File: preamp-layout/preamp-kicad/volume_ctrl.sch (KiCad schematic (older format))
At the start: 82 parts, among them J38 Conn_01x03_Male, J50 Conn_01x03_Male, J51 Conn_01x02_Male, J52 Conn_01x03_Male, J54 Conn_01x03_Male, J55 Conn_01x02_Male, J56 Conn_01x03_Male, J57 Conn_01x02_Male, U11 DAC5574, U12 TL074CDR, U13 NJM2068M, U14 THAT2181, U15 THAT2181, U16 NJM2068M, U17 THAT2181, U18 THAT2181

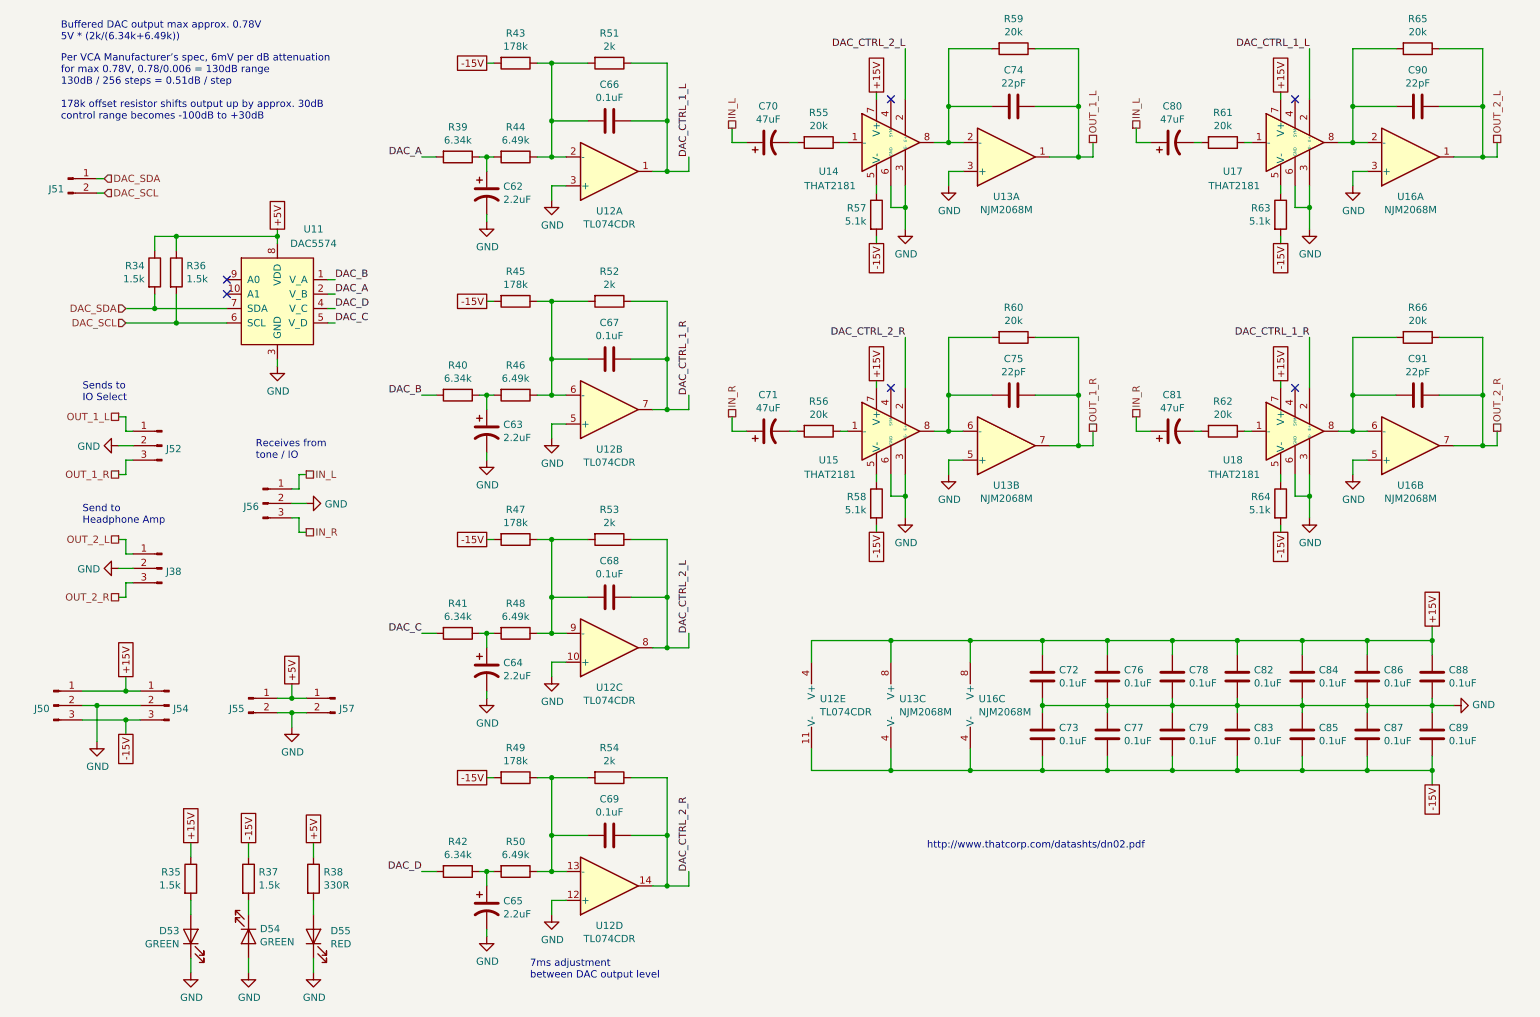
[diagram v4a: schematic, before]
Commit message: Balanced in/out update
Created THAT1646, THAT1280 schematic symbols an implemented in the balanced IO daughter card. Various layout updates as well, this is WIP.
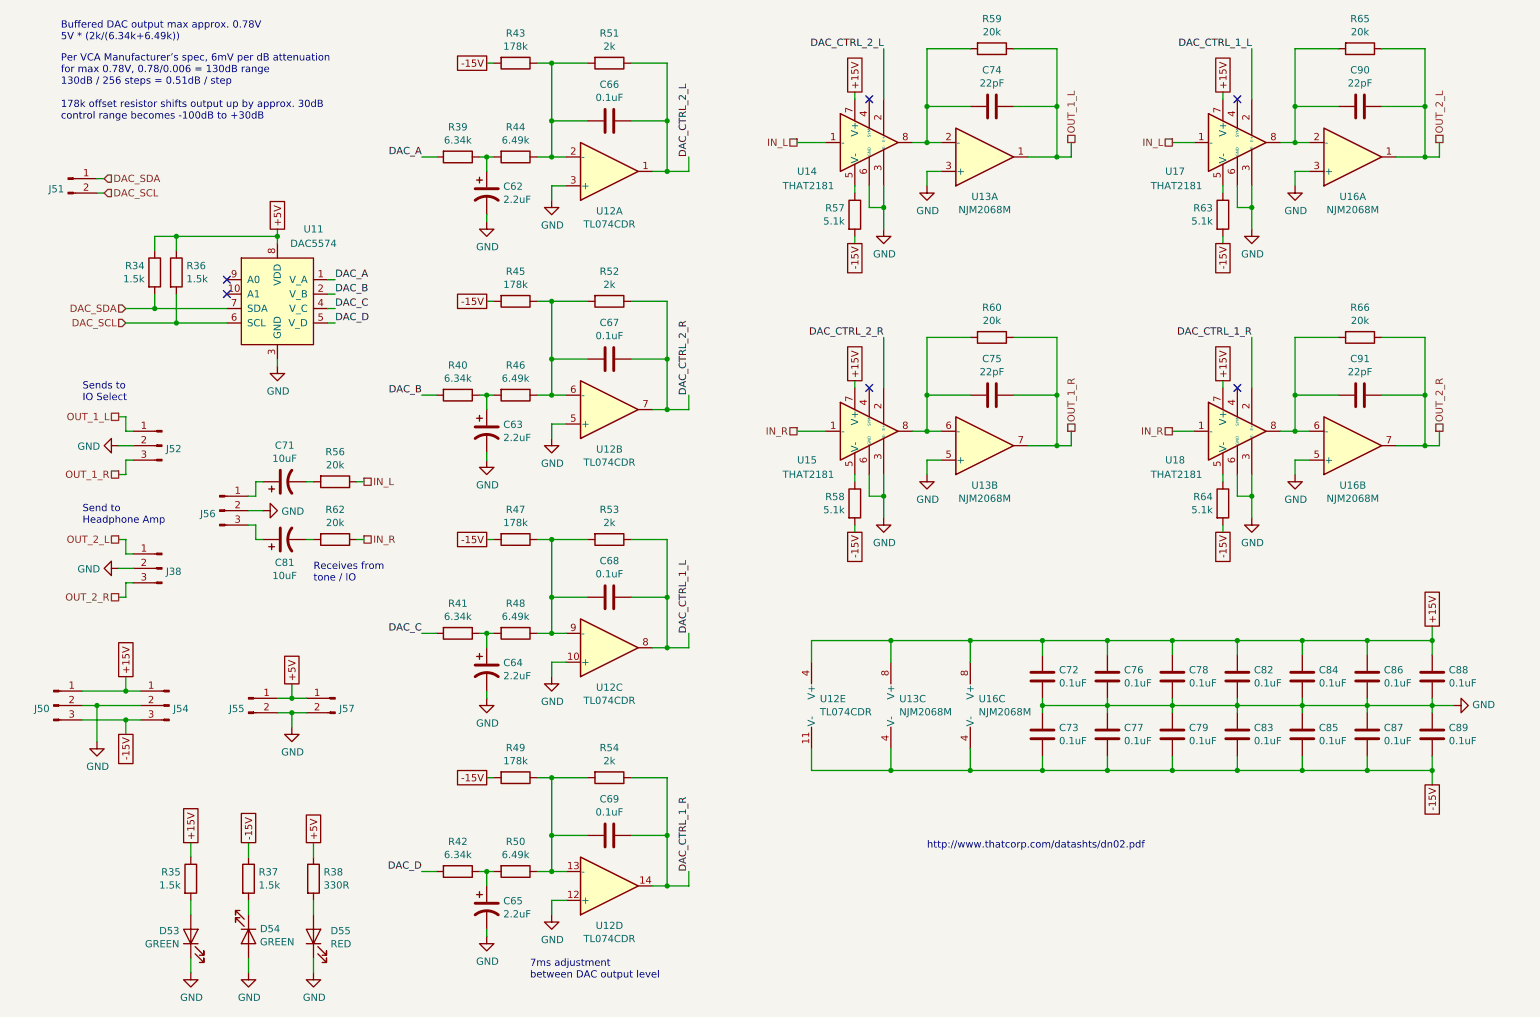
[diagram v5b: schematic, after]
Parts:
- removed C70, C80: 47uF, Capacitor_SMD:CP_Elec_6.3x5.4, symbol Device:CP1
- removed R55, R61: 20k, Resistor_SMD:R_1206_3216Metric_Pad1.42x1.75mm_HandSolder, symbol Device:R
- C71, C81: value 47uF -> 10uF; footprint Capacitor_SMD:CP_Elec_6.3x5.4 -> Capacitor_SMD:CP_Elec_4x5.4
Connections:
- net DAC_A: now also U11.1 (V_A); no longer U11.2 (V_B)
- net DAC_B: now also U11.2 (V_B); no longer U11.1 (V_A)
- net DAC_C: now also U11.4 (V_C); no longer U11.5 (V_D)
- net DAC_CTRL_1_L: now also C68.1, R53.1, U12.8; no longer C66.1, R51.1, U12.1
- net DAC_CTRL_1_R: now also C69.1, R54.1, U12.14; no longer C67.1, R52.1, U12.7
- net DAC_CTRL_2_L: now also C66.1, R51.1, U12.1; no longer C68.1, R53.1, U12.8
- net DAC_CTRL_2_R: now also C67.1, R52.1, U12.7; no longer C69.1, R54.1, U12.14
- net DAC_D: now also U11.5 (V_D); no longer U11.4 (V_C)
- net IN_L: now also R56.1, U14.1 (-), U17.1 (-); no longer J56.1 (Pin_1)
- net IN_R: now also R62.1, U15.1 (-), U18.1 (-); no longer C71.1, C81.1, J56.3 (Pin_3)
- new net: C71.1, J56.1 (Pin_1)
- new net: C81.1, J56.3 (Pin_3)
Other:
- moved on the sheet: C71, C74, C75, C81, C90, C91, J56, R56, R57, R58, R59, R60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

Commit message: PCB layout
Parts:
- removed J50, J54: Conn_01x03_Male, Connector_JST:JST_EH_S3B-EH_1x03_P2.50mm_Horizontal, symbol Connector:Conn_01x03_Male
- removed J55, J57: Conn_01x02_Male, Connector_JST:JST_EH_S2B-EH_1x02_P2.50mm_Horizontal, symbol Connector:Conn_01x02_Male
- removed U12: TL074CDR, Package_SO:SOIC-14_3.9x8.7mm_P1.27mm, symbol Amplifier_Operational:TL074
- added C2, C3: 0.1uF, Capacitor_SMD:C_1206_3216Metric_Pad1.42x1.75mm_HandSolder, symbol Device:C
- added J40, J41: Conn_01x04_Male, Connector_JST:JST_EH_S4B-EH_1x04_P2.50mm_Horizontal, symbol Connector:Conn_01x04_Male
- added U1, U2: TL072, Package_SO:SOIC-8_3.9x4.9mm_P1.27mm, symbol Amplifier_Operational:TL072
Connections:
- net +15V: now also C2.1, J40.1 (Pin_1), J41.1 (Pin_1), U1.8 (V+), U2.8 (V+)
- net +5V: now also J40.4 (Pin_4), J41.4 (Pin_4)
- net -15V: now also C3.2, J40.2 (Pin_2), J41.2 (Pin_2), U1.4 (V-), U2.4 (V-)
- net DAC_CTRL_1_L: now also U2.1
- net DAC_CTRL_1_R: now also U2.7
- net DAC_CTRL_2_L: now also U1.1
- net DAC_CTRL_2_R: now also U1.7
- net GND: now also J38.3 (Pin_3), J52.3 (Pin_3), J56.3 (Pin_3), C2.2, C3.1, J40.3 (Pin_3), J41.3 (Pin_3), U1.3 (+), U1.5 (+), U2.3 (+), U2.5 (+); no longer J38.2 (Pin_2), J52.2 (Pin_2), J56.2 (Pin_2)
- net IN_L: now also C71.1, J56.1 (Pin_1); no longer R56.1, U14.1 (-), U17.1 (-)
- net IN_R: now also C81.1, J56.2 (Pin_2); no longer R62.1, U15.1 (-), U18.1 (-)
- net OUT_1_L: now also U13.7; no longer U13.1
- net OUT_1_R: now also J52.2 (Pin_2), U13.1; no longer J52.3 (Pin_3), U13.7
- net OUT_2_L: now also U16.7; no longer U16.1
- net OUT_2_R: now also J38.2 (Pin_2), U16.1; no longer J38.3 (Pin_3), U16.7
- net at C66.2, R43.1, R44.1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: now also U1.2 (-)
- net at C67.2, R45.1, R46.1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: now also U1.6 (-)
- net at C68.2, R47.1, R48.1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: now also U2.2 (-)
- net at C69.2, R49.1, R50.1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: now also U2.6 (-)
- net at C74.2, R59.2, U14.8: now also U13.6 (-); no longer U13.2 (-)
- net at C62.1, R44.2: now also R42.1; no longer R39.1
- net at C63.1, R46.2: now also R39.1; no longer R40.1
- net at C75.2, R60.2, U15.8: now also U13.2 (-); no longer U13.6 (-)
- net at C90.2, R65.2, U17.8: now also U16.6 (-); no longer U16.2 (-)
- net at C65.1, R50.2: now also R40.1; no longer R42.1
- net at C91.2, R66.2, U18.8: now also U16.2 (-); no longer U16.6 (-)
- new net A_IN_L: R56.1, U14.1 (-), U17.1 (-)
- new net A_IN_R: R62.1, U15.1 (-), U18.1 (-)
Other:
- moved on the sheet: C71, C72, C73, C76, C77, C78, C79, C81, C82, C83, C84, C85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

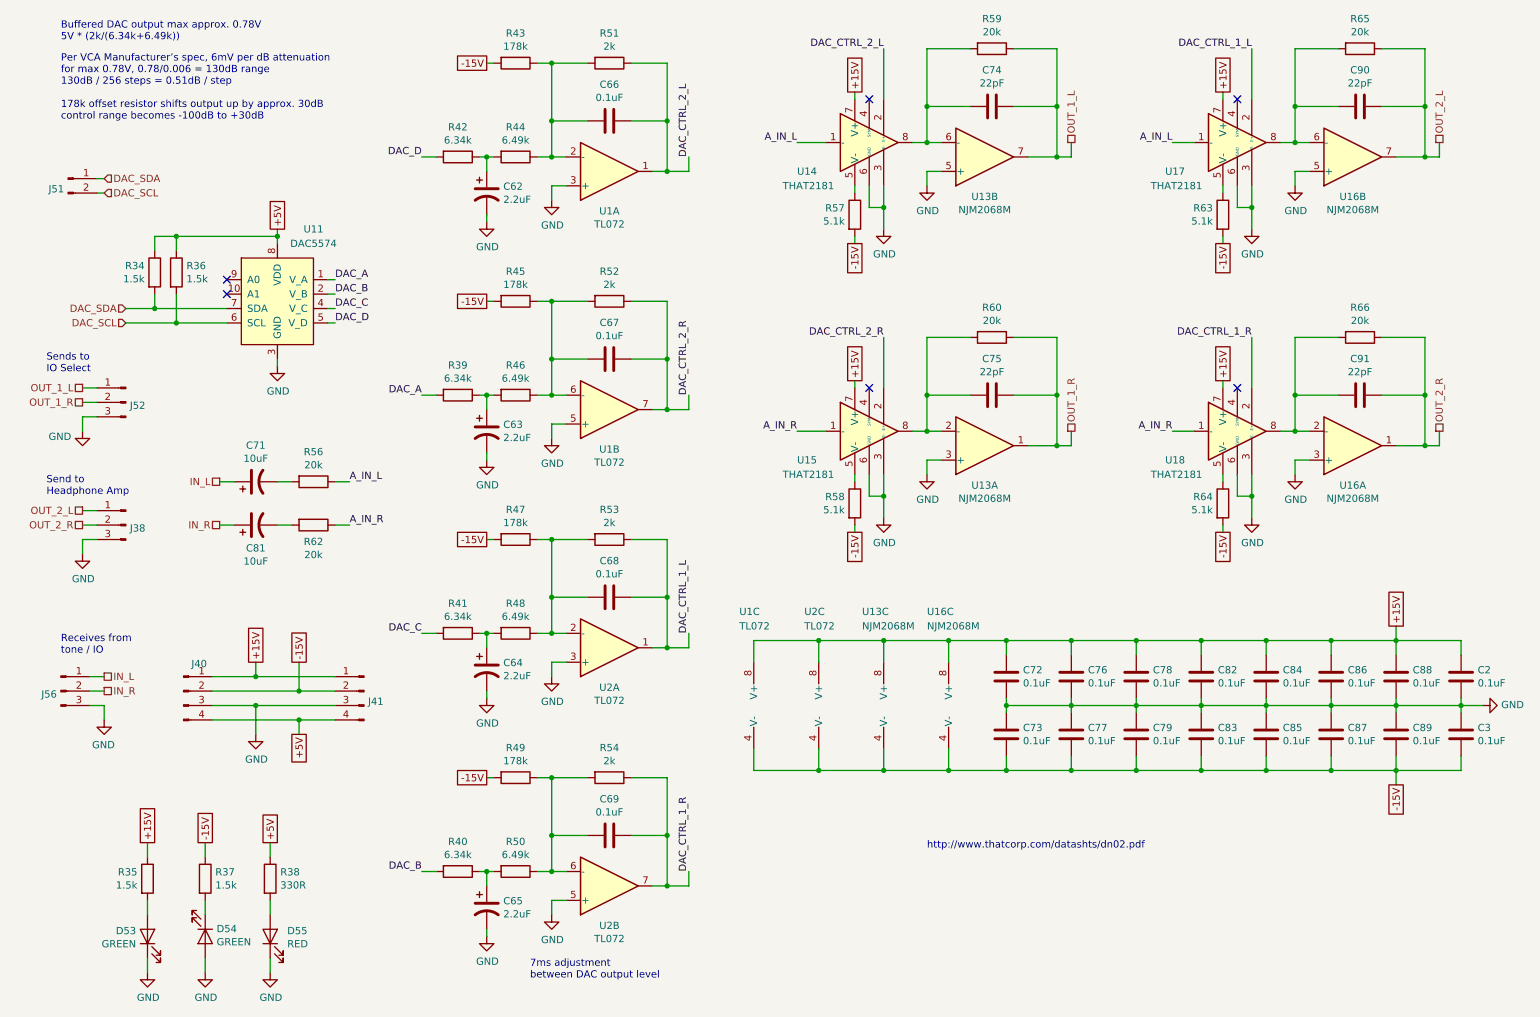
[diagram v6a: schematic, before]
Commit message: PCB layout update, front panel and LED restructure
Restructure of capacitive buttons. Restructure of MCU schematic. Moved LEDs to front panel sheet. Front panel and MCU initial PCB layout. 8 bit DAC update (grounded address pins). DAC connection renaming. Added mounting holes for boards.
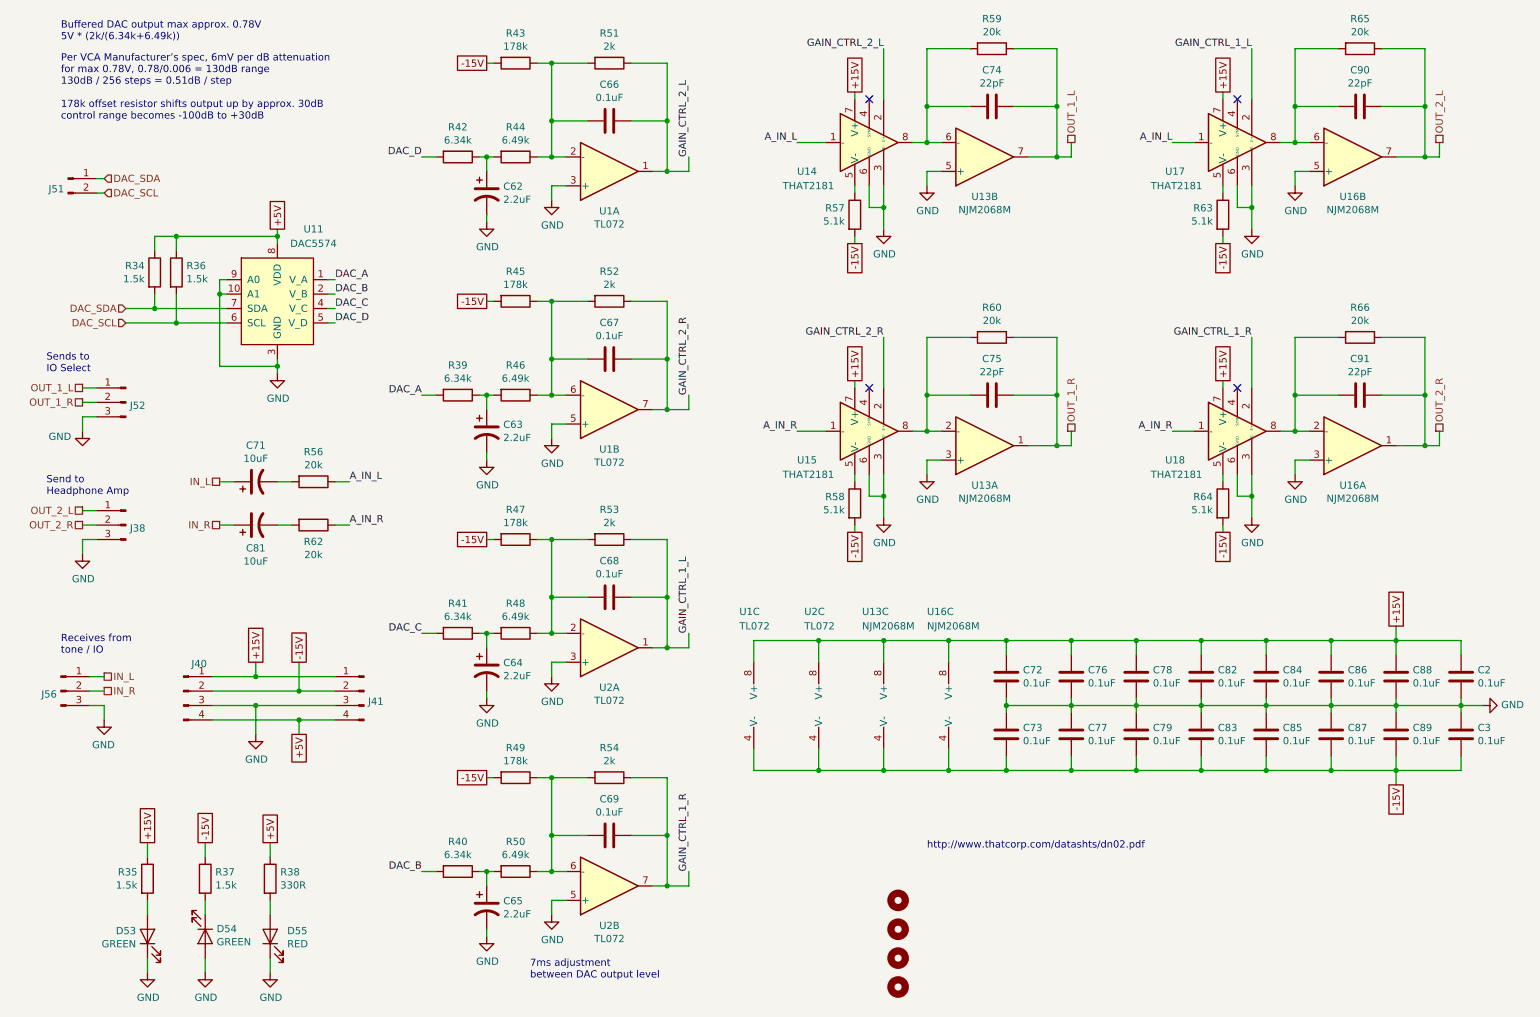
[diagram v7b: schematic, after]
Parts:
- added H21, H22, H23, H24: MountingHole, MountingHole:MountingHole_3.2mm_M3, symbol Mechanical:MountingHole
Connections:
- net GND: now also U11.10 (A1), U11.9 (A0)
- net DAC_CTRL_1_L renamed GAIN_CTRL_1_L
- net DAC_CTRL_1_R renamed GAIN_CTRL_1_R
- net DAC_CTRL_2_L renamed GAIN_CTRL_2_L
- net DAC_CTRL_2_R renamed GAIN_CTRL_2_R
- no-connect marks 6 -> 4
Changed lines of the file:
@@
 	6700 1300 6700 950
 Text Label 9250 950  2    50   ~ 0
-DAC_CTRL_1_L
+GAIN_CTRL_1_L
 Text Label 9250 2950 2    50   ~ 0
-DAC_CTRL_1_R
+GAIN_CTRL_1_R
 Text Label 6700 2950 2    50   ~ 0
-DAC_CTRL_2_R
+GAIN_CTRL_2_R
 Wire Wire Line
 	8000 1600 8000 1700
@@
 L power:GND #PWR067
 U 1 1 618BF574
-P 2500 3150
-F 0 "#PWR067" H 2500 2900 50  0001 C CNN
-F 1 "GND" H 2505 2977 50  0000 C CNN
-F 2 "" H 2500 3150 50  0001 C CNN
-F 3 "" H 2500 3150 50  0001 C CNN
-	1    2500 3150
-	1    0    0    -1
-$EndComp
-Wire Wire Line
-	2500 3100 2500 3150
-NoConn ~ 2150 2550
-NoConn ~ 2150 2650
+P 2500 3200
+F 0 "#PWR067" H 2500 2950 50  0001 C CNN
+F 1 "GND" H 2505 3027 50  0000 C CNN
+F 2 "" H 2500 3200 50  0001 C CNN
+F 3 "" H 2500 3200 50  0001 C CNN
+	1    2500 3200
+	1    0    0    -1
+$EndComp
 $Comp
 L Connector:Conn_01x02_Male J?
@@
 $EndComp
 Text Label 6700 950  2    50   ~ 0
-DAC_CTRL_2_L
+GAIN_CTRL_2_L
 Wire Wire Line
 	8700 1600 8850 1600
@@
 	6100 3600 6300 3600
 Text Label 5350 6650 1    50   ~ 0
-DAC_CTRL_1_R
+GAIN_CTRL_1_R
 Text Label 5350 3350 1    50   ~ 0
-DAC_CTRL_2_R
+GAIN_CTRL_2_R
 Text Label 5350 5000 1    50   ~ 0
-DAC_CTRL_1_L
+GAIN_CTRL_1_L
 Text Label 5350 1700 1    50   ~ 0
-DAC_CTRL_2_L
+GAIN_CTRL_2_L
 $Comp
 L Connector:Conn_01x04_Male J?
@@
 Wire Wire Line
 	3500 6650 3600 6650
+$Comp
+L Mechanical:MountingHole H?
+U 1 1 5EDF4915
+P 6800 6850
+AR Path="/5EDF4915" Ref="H?"  Part="1"
+AR Path="/5E2D8DA2/5EDF4915" Ref="H?"  Part="1"
+AR Path="/6009D432/5EDF4915" Ref="H21"  Part="1"
+F 0 "H21" H 6900 6850 50  0001 L CNN
+F 1 "MountingHole" H 6900 6805 50  0001 L CNN
+F 2 "MountingHole:MountingHole_3.2mm_M3" H 6800 6850 50  0001 C CNN
+F 3 "~" H 6800 6850 50  0001 C CNN
+	1    6800 6850
+	1    0    0    -1
+$EndComp
+$Comp
+L Mechanical:MountingHole H?
+U 1 1 5EDF491B
+P 6800 7050
+AR Path="/5EDF491B" Ref="H?"  Part="1"
+AR Path="/5E2D8DA2/5EDF491B" Ref="H?"  Part="1"
+AR Path="/6009D432/5EDF491B" Ref="H22"  Part="1"
+F 0 "H22" H 6900 7050 50  0001 L CNN
+F 1 "MountingHole" H 6900 7005 50  0001 L CNN
+F 2 "MountingHole:MountingHole_3.2mm_M3" H 6800 7050 50  0001 C CNN
+F 3 "~" H 6800 7050 50  0001 C CNN
+	1    6800 7050
+	1    0    0    -1
+$EndComp
+$Comp
+L Mechanical:MountingHole H?
+U 1 1 5EDF4921
+P 6800 7250
+AR Path="/5EDF4921" Ref="H?"  Part="1"
+AR Path="/5E2D8DA2/5EDF4921" Ref="H?"  Part="1"
+AR Path="/6009D432/5EDF4921" Ref="H23"  Part="1"
+F 0 "H23" H 6900 7250 50  0001 L CNN
+F 1 "MountingHole" H 6900 7205 50  0001 L CNN
+F 2 "MountingHole:MountingHole_3.2mm_M3" H 6800 7250 50  0001 C CNN
+F 3 "~" H 6800 7250 50  0001 C CNN
+	1    6800 7250
+	1    0    0    -1
+$EndComp
+$Comp
+L Mechanical:MountingHole H?
+U 1 1 5EDF4927
+P 6800 7450
+AR Path="/5EDF4927" Ref="H?"  Part="1"
+AR Path="/5E2D8DA2/5EDF4927" Ref="H?"  Part="1"
+AR Path="/6009D432/5EDF4927" Ref="H24"  Part="1"
+F 0 "H24" H 6900 7450 50  0001 L CNN
+F 1 "MountingHole" H 6900 7405 50  0001 L CNN
+F 2 "MountingHole:MountingHole_3.2mm_M3" H 6800 7450 50  0001 C CNN
+F 3 "~" H 6800 7450 50  0001 C CNN
+	1    6800 7450
+	1    0    0    -1
+$EndComp
+Wire Wire Line
+	2500 3100 2500 3150
+Wire Wire Line
+	2500 3150 2100 3150
+Wire Wire Line
+	2100 3150 2100 2650
+Wire Wire Line
+	2100 2550 2150 2550
+Connection ~ 2500 3150
+Wire Wire Line
+	2500 3150 2500 3200
+Wire Wire Line
+	2150 2650 2100 2650
+Connection ~ 2100 2650
+Wire Wire Line
+	2100 2650 2100 2550
 $EndSCHEMATC
